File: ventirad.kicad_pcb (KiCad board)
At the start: 2 copper layers, 50 x 100 mm, 101 parts, among them Q1 2N7000, Q10 IRFR9014, Q11 2N7000, Q12 IRFR9014, Q13 2N7000, Q14 2N7000, Q15 2N7000, Q16 2N7000, Q17 2N7000, Q18 2N7000, Q2 IRFR9014, Q3 2N7000, Q4 IRFR9014, Q5 2N7000, Q6 IRFR9014, Q7 2N7000, Q8 IRFR9014, Q9 2N7000, U1 LM7805, U2 http://wiki.electrolab.fr/Pro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

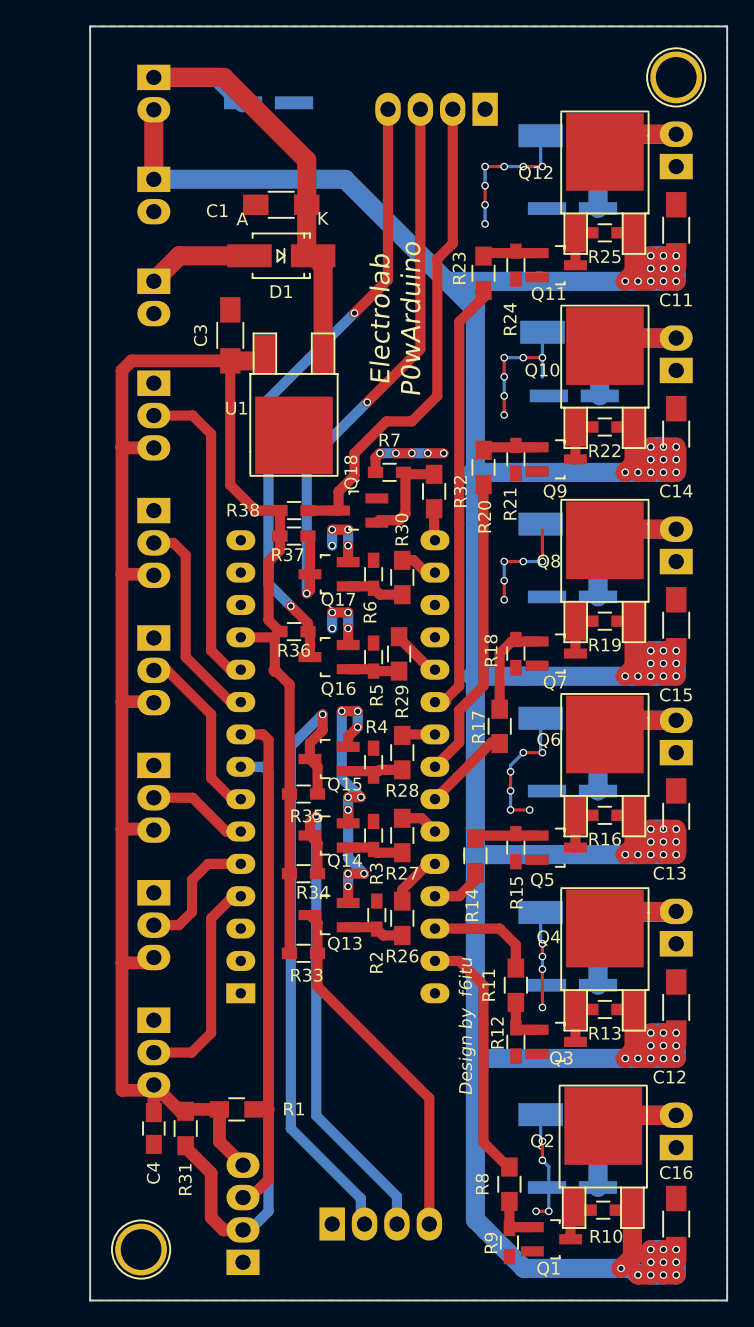
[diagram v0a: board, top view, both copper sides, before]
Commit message: version Shielded et empreinte capapol elargies
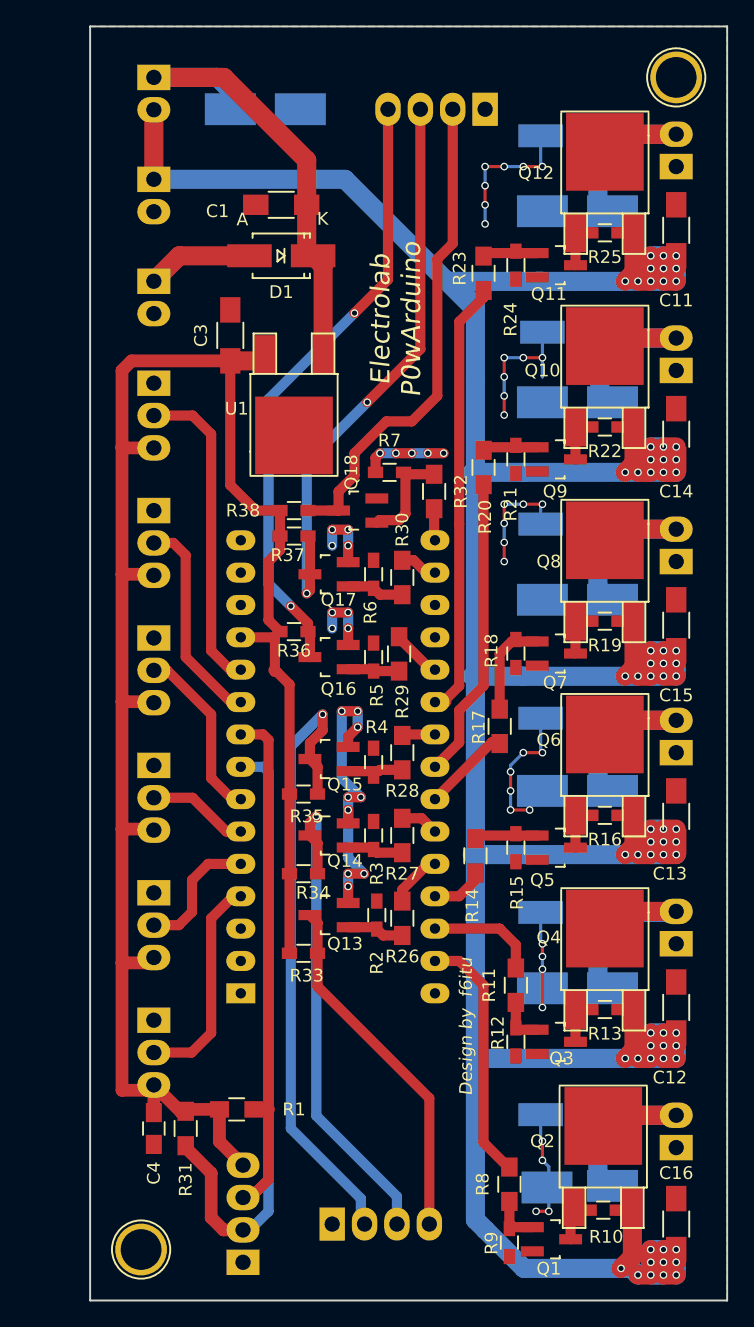
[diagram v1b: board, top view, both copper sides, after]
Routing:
- net GND: track 100.1 -> 100.7 mm, vias 54 -> 55

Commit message: lib cleaning, mounting holes
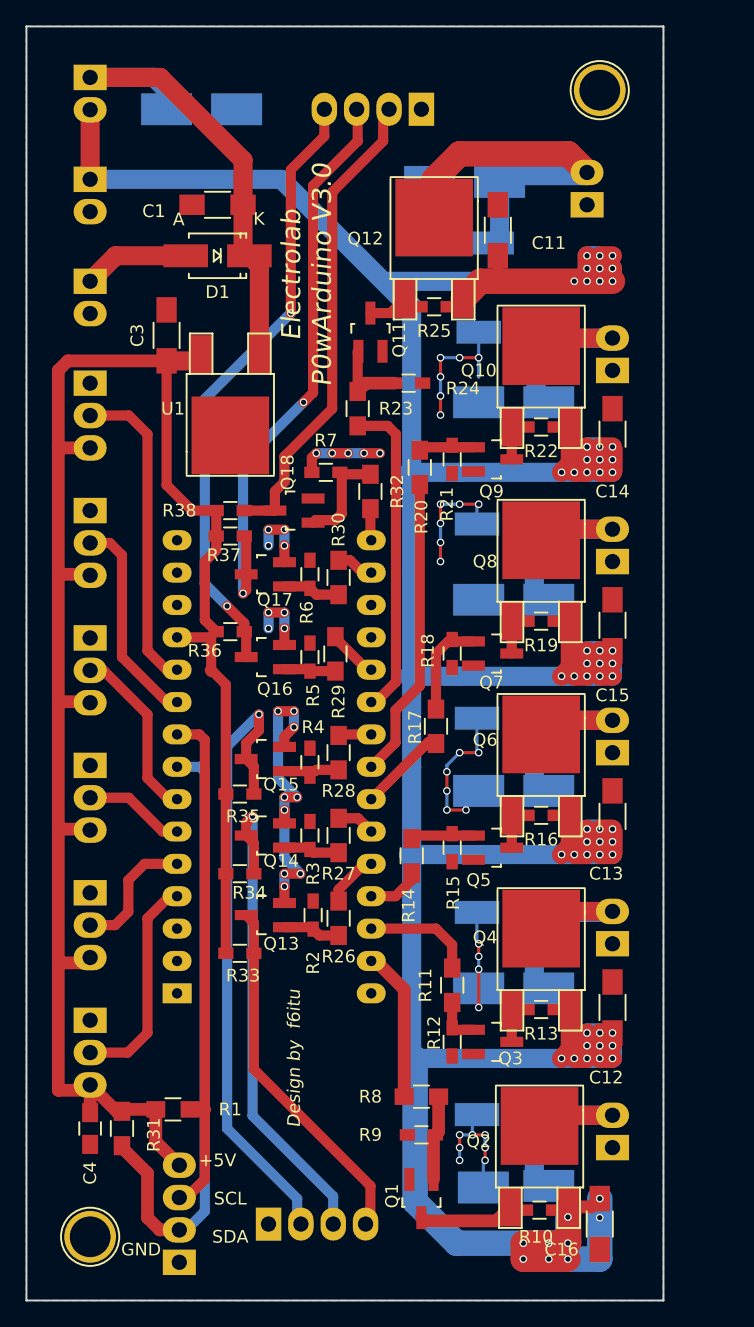
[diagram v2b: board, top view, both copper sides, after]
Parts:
- moved Q11 15.5 mm to (134.0, 84.0), turned to 0 degrees
- moved R25 14.6 mm to (139.0, 82.0)
- moved R23 14.5 mm to (133.0, 90.0)
- moved Q12 14.4 mm to (139.0, 81.3)
- moved C11 14.0 mm to (144.0, 76.0)
- moved R24 12.5 mm to (137.0, 88.0), turned to 0 degrees
- moved D7 12.2 mm to (141.0, 77.0)
- moved R9 10.9 mm to (138.0, 147.0), turned to 180 degrees
- moved Q1 10.7 mm to (138.0, 152.0), turned to 180 degrees
- moved R8 9.75 mm to (138.0, 144.0), turned to 180 degrees
- moved C10 9.15 mm to (141.0, 72.0)
- moved ? 7.62 mm to (151.0, 74.0)
- moved ? 6.08 mm to (152.0, 65.0)
- moved C16 6.00 mm to (152.0, 154.0), turned to 90 degrees
- moved ? 5.00 mm to (112.0, 64.0)
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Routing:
- net Net-(C11-Pad2): track 284.8 -> 300.8 mm, vias 66 -> 63
- net Net-(C10-Pad1): track 17.8 -> 28.7 mm
- net GND: track 100.7 -> 90.3 mm, vias 55 -> 51
- net Net-(R23-Pad2): track 35.2 -> 25.3 mm
- net Net-(R8-Pad2): track 19.8 -> 11.9 mm
- net Net-(Q1-Pad3): track 4.10 -> 9.38 mm
- net Net-(Q1-Pad1): track 4.28 -> 6.66 mm
- net Net-(Q11-Pad1): track 4.35 -> 6.69 mm
- net Net-(P18-Pad2): track 38.8 -> 37.6 mm
- net Net-(Q11-Pad3): track 3.89 -> 4.65 mm
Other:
- board text added: "+5V"
- board text added: "Electrolab P0wArduino V3.0"
- board text removed: "Electrolab P0wArduino"

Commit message: some file refresh and ibom, kicad 7 files
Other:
- net class Default removed
